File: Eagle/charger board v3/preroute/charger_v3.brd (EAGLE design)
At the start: 98.7 x 90.2 mm, 37 parts, among them IC1 IR2110D, Q2 IRFP240, Q3 MJE13003G

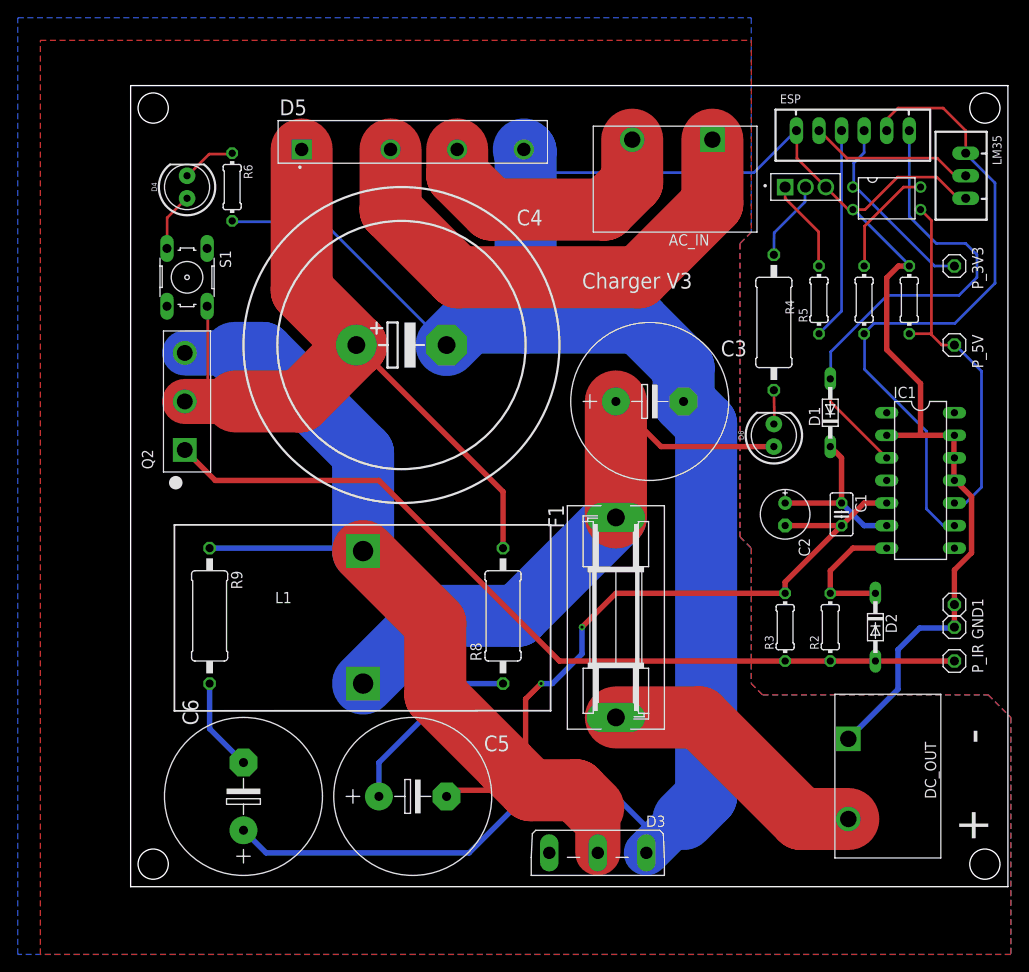
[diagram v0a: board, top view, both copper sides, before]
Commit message: routing v3
routing v3: opto, snubber, momentary pb, fuse adjst
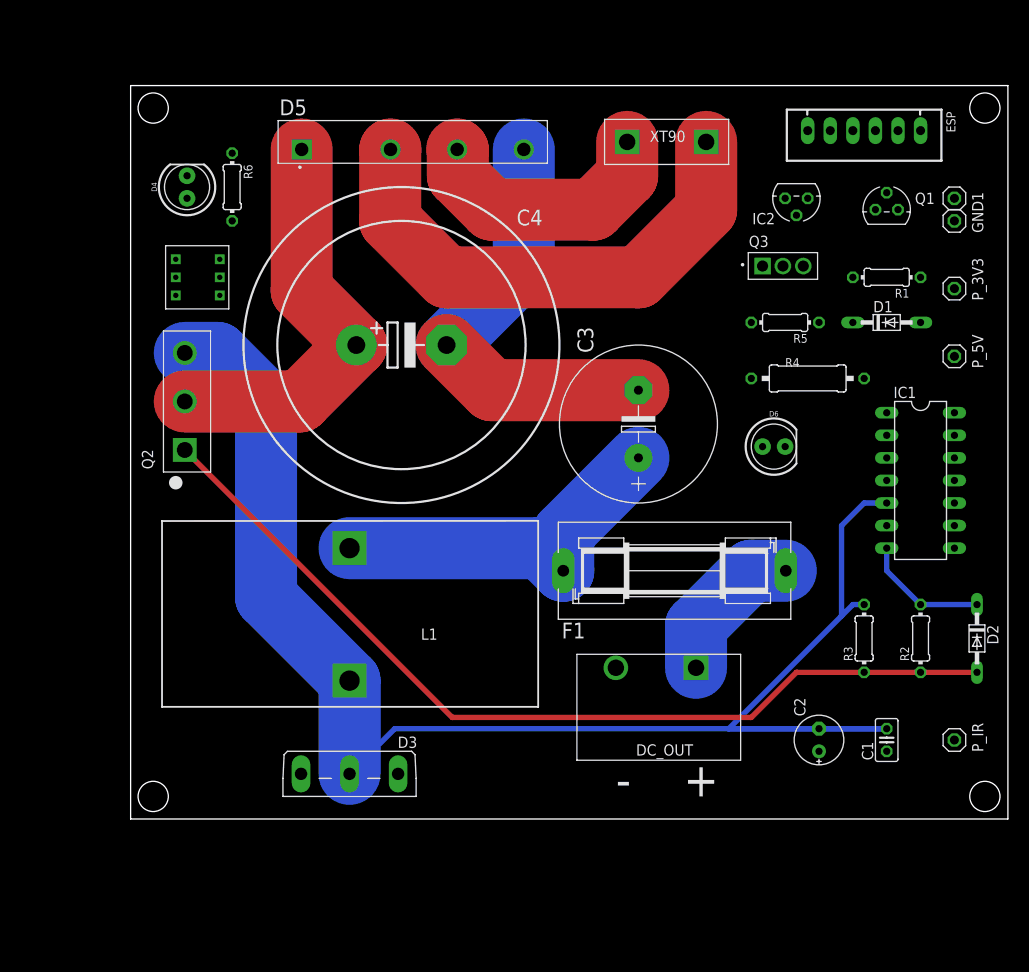
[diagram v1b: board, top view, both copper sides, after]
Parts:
- removed C5, C6: 22uF, rcl:E7,5-18
- removed LM35: JST-XH-03-PIN-LONG-PAD, Rembrandt Electronics - JST XH Connectors v1-0:JST-XH-03-PACKAGE-LONG-PAD
- removed OK1: SFH618A-5, optocoupler:DIP4
- removed R7: 1k, rcl:0204/7
- removed R8, R9: 31, rcl:0411/15
- removed S1: (no value), switch-omron:B3F-10XX
- added IC2: LM35CZ, lm35:TO92
- added Q1: 2N7000, 2N7000:TO92
- added U$1: SWITCH-DPDT-7X7A, TA_library:TL-2230
- AC_IN: value 1977477-2 -> XT90A; device terminal_block_TA:TE_1977477-2 -> TA_library:XT90-PAD
- F1: device TA_library:FUSEHOLDER -> fuse:SH25
- R1: value 180 -> 10k
- R4: device rcl:0411/15 -> rcl:0309/12
- moved GND2 48.3 mm to (92.7, 69.8)
- moved GND1 43.2 mm to (92.7, 67.3)
- moved D3 29.3 mm to (24.6, 2.54)
- moved DC_OUT 26.4 mm to (60.4, 11.7), turned to 180 degrees
- moved C1 25.9 mm to (85.1, 8.89), turned to 90 degrees
- moved C2 25.7 mm to (77.5, 8.89), turned to 90 degrees
- moved D1 12.0 mm to (85.1, 55.9), turned to 0 degrees
- moved D2 11.5 mm to (95.2, 20.3)
- moved R2 10.2 mm to (88.9, 20.3)
- moved Q3 9.25 mm to (71.1, 62.2)
- moved R3 8.98 mm to (82.5, 20.3)
- moved P_IR 8.89 mm to (92.7, 8.89)
- moved F1 8.44 mm to (61.2, 27.9), turned to 0 degrees
- moved L1 8.28 mm to (29.5, 22.1), turned to 90 degrees
- moved R4 7.36 mm to (76.2, 49.6), turned to 0 degrees
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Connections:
- removed net N$11: OK1.4, R1.2
- removed net N$6: C5.+, R8.1
- removed net N$7: C6.-, R9.2
- net 5V: now also IC2.1, R1.2; no longer LM35.3, R1.1
- net AC_1: now also AC_IN.P$1; no longer AC_IN.1
- net AC_2: now also AC_IN.P$2; no longer AC_IN.2
- net GND: now also DC_OUT.2, IC2.3, Q1.1; no longer C6.+, DC_OUT.1, LM35.1, OK1.2, R7.1
- net HVDC: now also U$1.1; no longer R8.2, S1.2
- net N$2: now also U$1.2; no longer S1.3
- net NMOS_SOURCE: no longer C5.-, R9.1
- net PWM_5V: now also Q1.3, R1.1; no longer OK1.3, R7.2
- net PWM_SW1: now also Q1.2; no longer OK1.1
- net TEMP: now also IC2.2; no longer LM35.2
- net V_OUT_FUSE: now also DC_OUT.1; no longer DC_OUT.2
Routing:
- net GND: track 345.4 -> 49.3 mm
- net 5V: track 73.9 -> 0.00 mm
- net 12V: track 56.2 -> 0.00 mm
- net HVDC: track 89.4 -> 46.5 mm
- net PWM_5V: track 41.2 -> 0.00 mm
- net V_OUT: track 69.1 -> 41.3 mm
- net PWM_SW2: track 23.9 -> 0.00 mm
- net PWM_SW1: track 22.0 -> 0.00 mm
- net N$6: track 21.5 -> 0.00 mm
- net VB: track 19.4 -> 0.00 mm
- net TEMP: track 18.6 -> 0.00 mm
- net V_OUT_FUSE: track 30.9 -> 17.4 mm
- net N$11: track 12.6 -> 0.00 mm
- net N$7: track 10.5 -> 0.00 mm
- net N$5: track 10.5 -> 0.00 mm
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- added copper zone on layer 16, net N$6
- removed copper zone on layer 1, net GND
- removed copper zone on layer 16, net GND
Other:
- board size 98.7 x 90.2 mm -> 98.7 x 82.5 mm
- board text removed: "Charger V3"
